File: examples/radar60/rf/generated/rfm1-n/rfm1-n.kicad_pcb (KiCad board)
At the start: 6 copper layers, 31.8 x 23.1 mm, 9 parts, among them U1 IWR6843AQGABLR (rings 0-2 of 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

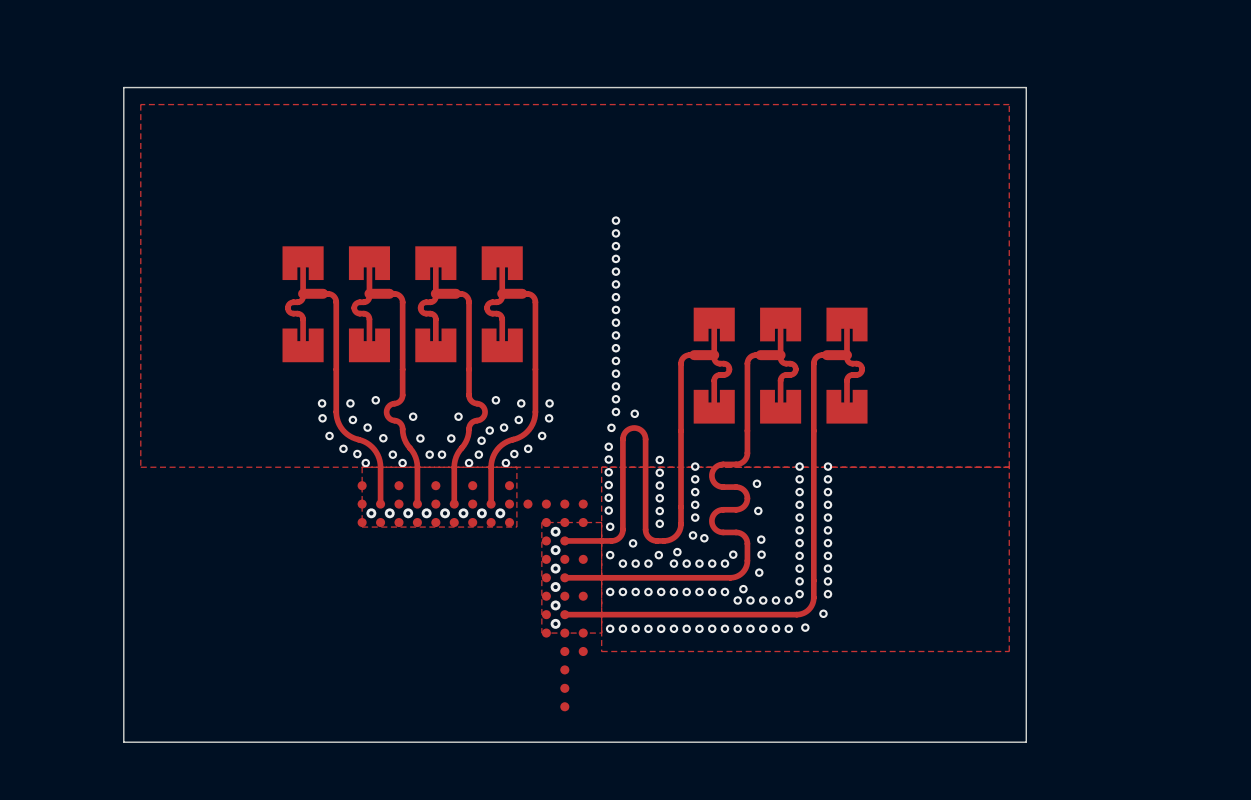
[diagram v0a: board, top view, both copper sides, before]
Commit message: radar60 rf: openEMS first validation and full-wave patch calibration
First EM validation of the conventional column (two patches on L2
windows, corporate divider, gap input) in openEMS v0.37.0-rc3 on the
Mac (Docker, 4 threads, 1.25 M cells, about 14 min per run; no GCP):

- as drawn from closed form the patch resonates at 60.0 GHz, not
  62.05 (-3.3 %), and the column never reaches RL 10 dB (best 9.2 dB at
  60.2 GHz); realized broadside gain 0.0 dBi at 62.05 GHz (7.4 at 60.3)
  against 9.2 dBi predicted;
- a via ring round each window (L2-L3 stitching) does not help;
- a three-point single-patch sweep (L x0.967, inset 0.30/0.38/0.45,
  picked by |S11| at 62.05 GHz) matches the patch (RL >= 10 dB
  60.90-62.80 GHz, -26.9 dB at 61.9 GHz); the column with it reaches
  6.3 / 7.7 / 6.9 dBi realized gain at 60.3 / 62.05 / 63.8 GHz,
  directivity 9.4 dBi, radiation efficiency 70-78 %, but its input is
  still mismatched in band (RL 5.9 / 9.1 / 11.4 dB), which C1 sizes.

The generator now draws L = closed-form L x 0.967 with inset 0.30 mm
(declared parameters citing results/openems/patch-c-i30); the D12
variants bracket the calibrated length. column_sim.py gains a matched
feed (Feed_R 50), a single-patch diagnostic and an optional window via
ring; summarize.py tabulates runs against the closed-form predictions.
All four boards regenerated; KiCad 10.0.6 DRC still reports no
violations and no unconnected items.

Co-Authored-By: Claude Opus 5.5 <noreply@anthropic.com>
Claude-Session: https://claude.ai/code/session_014FiHUDEn5jCP4V8pPjQkPy
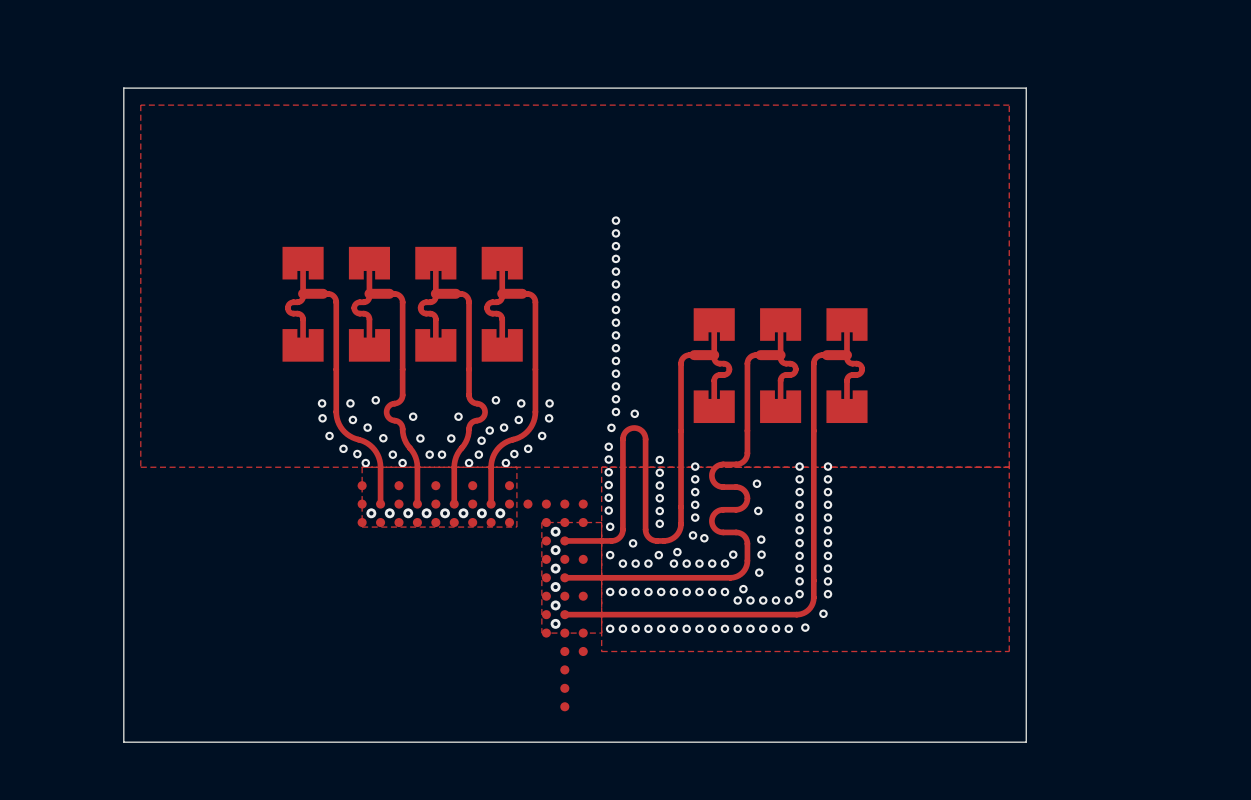
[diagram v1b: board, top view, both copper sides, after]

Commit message: radar60 rf: review fixes (via rules, In2 clip, L2-L3 stitching, placeholder status)
- Fence and isolation vias 0.15/0.32 (the profile's 3 mil ring) with no two vias closer than
  0.43 mm (11 mil hole to hole); the coupon strip likewise. Integration DRC found 288 via and
  2 hole-to-hole violations with the old 0.30 pad and 0.40 spacing.
- In2.Cu GND only where the macro needs its L3 reference: the RF region outside the package,
  the under-package ground of rows 1-3 and A-C, and each land's L2 cut-out plus 0.3 mm. Under
  the rest of the package In2 is the board's escape layer. The outlines go into each record
  (board_frame.in2_gnd_polygons) for the fanout. The macro region now starts at the east pour
  (U1 y -1.3), as the board's RF region does.
- L2-L3 stitching: 208 GND through vias every 0.6 mm (lambda_d/4 in RO4450F at 62 GHz is
  0.64 mm) round each bank (1.4 mm from the patches) and inside the In2 GND boundary. Not
  simulated yet: the C2 bank solve has to report it.
- Every record carries status "placeholder": the column fails ANT-02 RL at P1 (col-c), the
  calibration came from one patch, C1 and C2 come before the macro is frozen.

rfm1-m/-n/-p and the coupon strip: KiCad DRC clean, no unconnected items.

Co-Authored-By: Claude Opus 5.5 <noreply@anthropic.com>
Claude-Session: https://claude.ai/code/session_014FiHUDEn5jCP4V8pPjQkPy
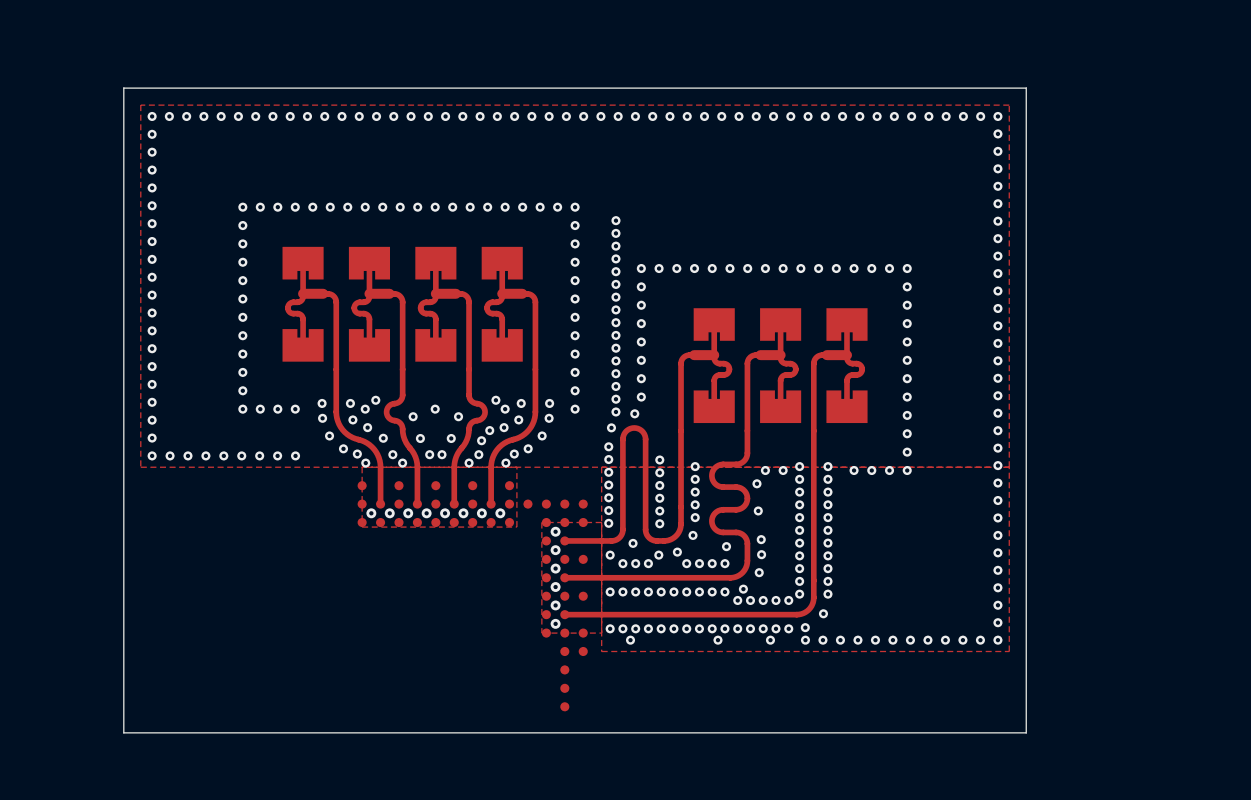
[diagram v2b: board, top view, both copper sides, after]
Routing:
- net GND: vias 158 -> 364
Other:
- board size 31.8 x 23.1 mm -> 31.8 x 22.7 mm

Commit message: radar60 rf: regenerate rfm1-m/n/p and the coupon strip; README
Generator checks pass for all three D12 variants (outside-cut-out hash
identical); kicad-cli pcb drc --refill-zones --severity-all: no
violations, no unconnected items on rfm1-m, -n, -p and the coupon strip.

board_frame (U1 at 26, 28) [D]: RX phase centres y 39.988 (x unchanged),
TX x 38.718 / 41.060 / 43.402 at y 38.100; cut-outs RX 16.599-32.205 x
36.688-43.024, TX 34.205-47.469 x 34.800-41.136; region x 12.599-51.469,
y 26.7-47.024; R4 guard x 7.599-56.469; board height >= 47.349; nearest
active RX-TX phase centres 11.19 mm; loads RL1-RL4.

README: new geometry, the uniformity rules, the checks, the floorplan, the
coupons, the audit and test commands; the integration (kicad_ops) still has
to take the dummy footprints and loads.

Co-Authored-By: Claude Opus 5.5 <noreply@anthropic.com>
Claude-Session: https://claude.ai/code/session_014FiHUDEn5jCP4V8pPjQkPy
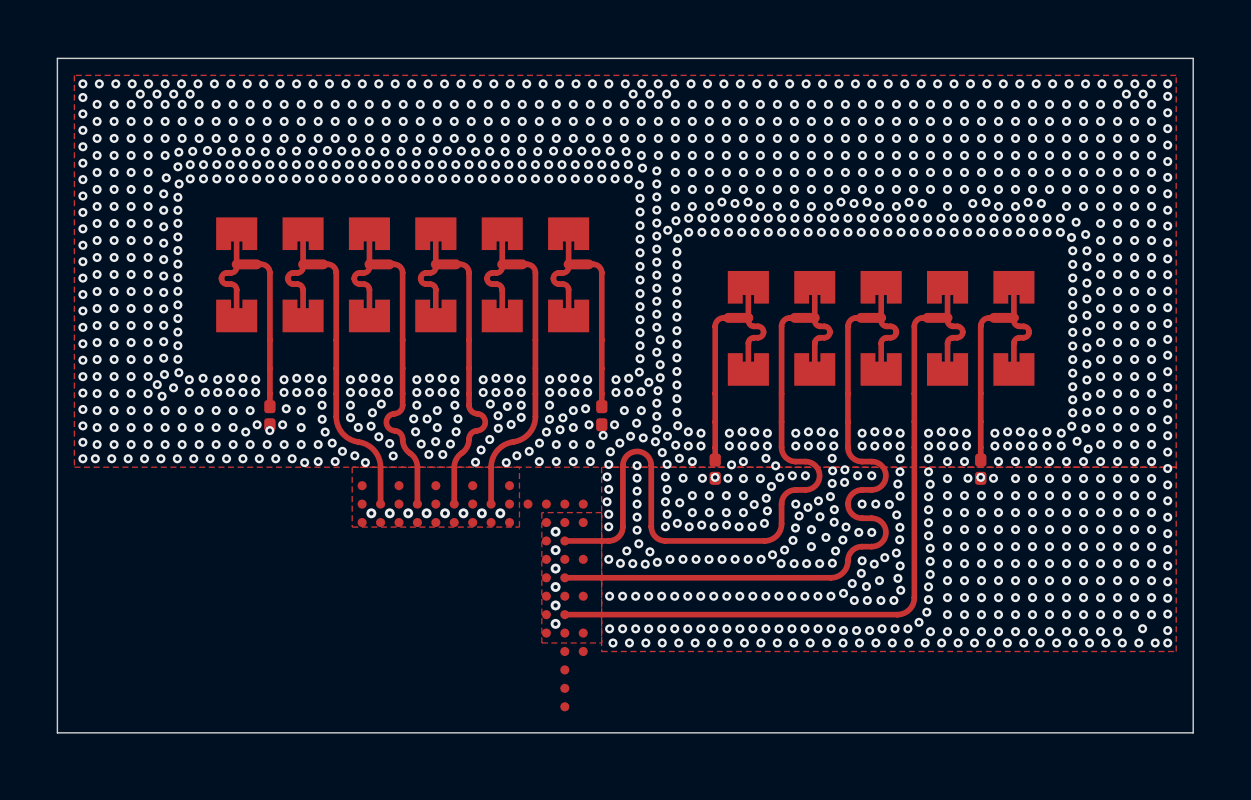
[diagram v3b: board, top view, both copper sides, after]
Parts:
- added ANT_RXD0: 2-patch corporate column, terminated dummy, radar60:COL2_DUMMY, F.Cu at (92.3, 88.0)
- added ANT_RXD5: 2-patch corporate column, terminated dummy, radar60:COL2_DUMMY, F.Cu at (104.0, 88.0)
- added ANT_TXD0: 2-patch corporate column, terminated dummy, radar60:COL2_DUMMY, F.Cu at (110.4, 89.9)
- added ANT_TXD4: 2-patch corporate column, terminated dummy, radar60:COL2_DUMMY, F.Cu at (119.7, 89.9)
- added RL1: 50R 0201 thin film, radar60:R_0201_0603Metric_LOAD, F.Cu at (93.5, 93.0)
- added RL2: 50R 0201 thin film, radar60:R_0201_0603Metric_LOAD, F.Cu at (105.2, 93.0)
- added RL3: 50R 0201 thin film, radar60:R_0201_0603Metric_LOAD, F.Cu at (109.2, 94.9)
- added RL4: 50R 0201 thin film, radar60:R_0201_0603Metric_LOAD, F.Cu at (118.6, 94.9)
- moved ANT_TX1 3.78 mm to (112.7, 89.9)
- moved ANT_TX2 3.78 mm to (115.1, 89.9)
- moved ANT_TX3 3.78 mm to (117.4, 89.9)
- moved ANT_RX1 1.04 mm to (94.7, 88.0)
- moved ANT_RX2 1.04 mm to (97.0, 88.0)
- moved ANT_RX3 1.04 mm to (99.3, 88.0)
- moved ANT_RX4 1.04 mm to (101.7, 88.0)
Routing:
- net RXD0: track 0.00 -> 9.10 mm
- net RXD5: track 0.00 -> 9.10 mm
- net TXD0: track 0.00 -> 9.10 mm
- net TXD4: track 0.00 -> 9.10 mm
- net TX3: track 21.7 -> 26.6 mm
- net TX2: track 21.4 -> 26.2 mm
- net TX1: track 21.6 -> 26.2 mm
- net RX1: track 12.2 -> 13.3 mm
- net RX4: track 12.2 -> 13.3 mm
- net RX2: track 12.1 -> 13.2 mm
- net RX3: track 12.1 -> 13.2 mm
- net GND: vias 364 -> 1443
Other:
- board size 31.8 x 22.7 mm -> 40.1 x 23.8 mm

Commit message: radar60 rf: review fixes of the RF-uniformity layout (loads, G2, G7, audit, coupons)
- Dummy loads: one load cell. Fill vias had landed in three of the four
  0201 GND lands (and differently in each). Each load now has its own five
  vias (pad edges >= 0.14 mm from either land), no other via in its via
  zone, a solder-mask island so the GND land is mask-defined and its vias
  tented, and references RT1-RT4 (RL1/RL2 are the board's radome lands).
  The lands are copper, not pour, for the stitch-reach check. New G7: the
  load cells are identical and no via comes within 0.10 mm of a land.
- G2: the congruence window is symmetric (+-(2d - W/2 - margin)) against
  an interior column. The one declared difference (the absent
  second-neighbour input at an open bank end, RX1 and TX3: 0.95 mm2 of
  copper, 2 vias) is masked and reported.
- Board audit: A1 measures a contact along the cut-out boundary (the x
  extent read TX1's 0.96 mm side contact as 0.05). A2 also compares In1
  and In2 and uses G2's window. New A6: vias at SMD lands. pcbnew is
  imported lazily, so the audits run in the unit tests.
- Regression fixture: the pre-fix rfm1-n (ab57757), KiCad-filled. A1-A4
  must fail on it (RX2/RX3 0.87 mm, TX2 1.48 mm, TX1 two contacts).
- Coupons: CP-T2 (TX2) joins CP-T/CP-T3; without it TX2's corridor was a
  1.3 mm GND channel with a TE10 cut-off near 63 GHz. CP-A gets the
  guard-band rows. The 60 GHz part of the strip is stitched (edge rows,
  0.6 mm grid, fill) and checked like G3. The loads sit under mask islands.
- Regenerated rfm1-m/n/p and the strip. KiCad DRC is clean on all four,
  and A1-A6 pass on the filled m, n and p.

Co-Authored-By: Claude Opus 5.5 <noreply@anthropic.com>
Claude-Session: https://claude.ai/code/session_014FiHUDEn5jCP4V8pPjQkPy
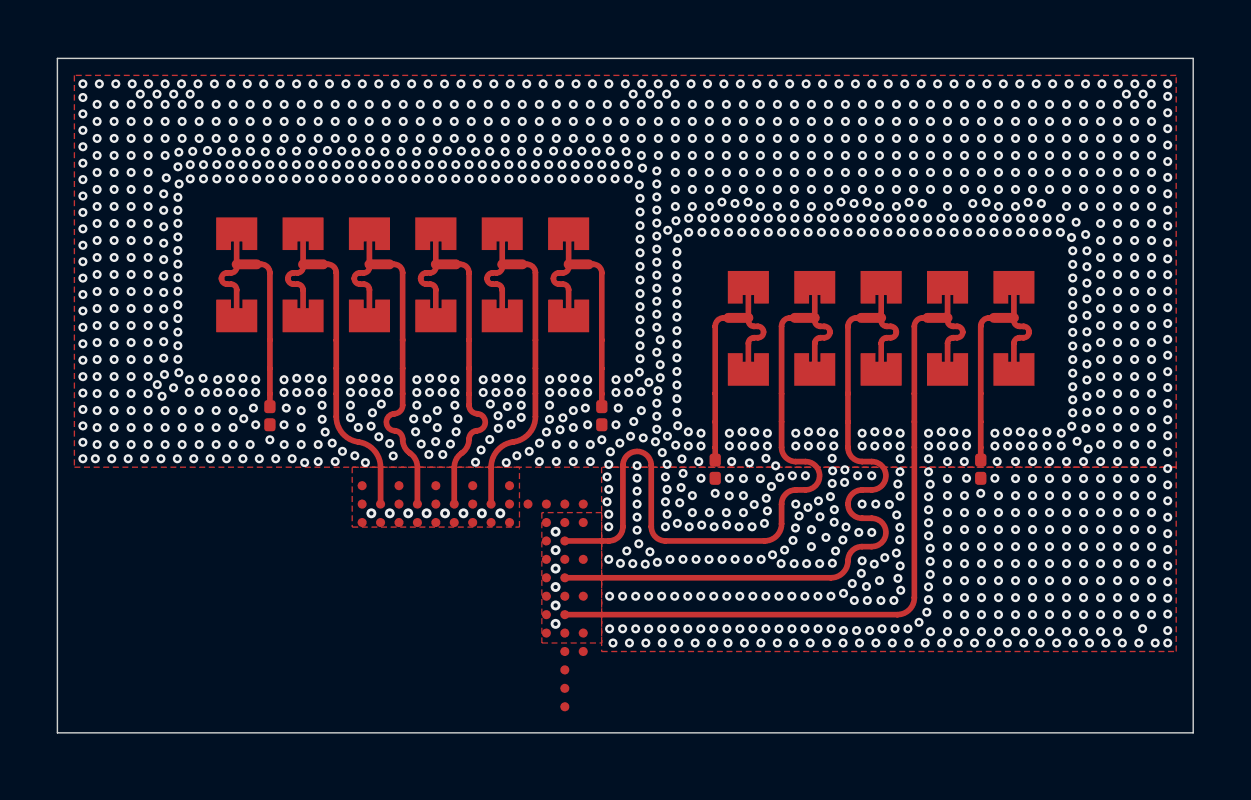
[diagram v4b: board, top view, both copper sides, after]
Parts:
- removed RL1, RL2, RL3, RL4: 50R 0201 thin film, radar60:R_0201_0603Metric_LOAD
- added RT1: 50R 0201 thin film, radar60:R_0201_0603Metric_LOAD, F.Cu at (93.5, 93.0)
- added RT2: 50R 0201 thin film, radar60:R_0201_0603Metric_LOAD, F.Cu at (105.2, 93.0)
- added RT3: 50R 0201 thin film, radar60:R_0201_0603Metric_LOAD, F.Cu at (109.2, 94.9)
- added RT4: 50R 0201 thin film, radar60:R_0201_0603Metric_LOAD, F.Cu at (118.6, 94.9)
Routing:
- net GND: vias 1443 -> 1441

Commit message: radar60 rf: stage 3b generator options, D14 PA feed, D15 pour variants, E1 models
Generator (examples/radar60/rf/rfmacro):
- D14: the macro owns the VOUT_PA (1V0_PA) feed: A2/B2 bar, a neck east of row A
  inside the package outline, four 0.20/0.40 vias in the pocket (board rules
  unchanged; PWR clearance 0.15 mm), an In3 tie stand-in, board_frame.pa_feed
  hand-off (skip_pads A2/B2). New check G8: clearances, pocket, L2 anti-pads,
  current per via, IR drop [D].
- D15: pour presets A (0.60 mm grid), B (1.00 mm grid, interior hard maximum
  0.75 mm), C (GCPW strips, rings, isolation, load cells; L2-L3 lattice). G3 has
  edge and interior thresholds and an L2-L3 check; stitch metrics per record.
- Dummies S1 / S1.5 and DNP loads ("short" refused); G2 declares the edge
  columns S1 leaves without a neighbour.
- L2-L3 cavity options K0 / K2 (posts, column-congruent) / K1; check G9.
- C1 / D5: div_l_scale and a series-fed column in the bank.
- TX: T2 (R 0.75 north-west finger), T4 (TX1 within a skew budget), T3 order
  planarity; the fit keeps lines out of load mask islands.
- Via placement closes fence gaps a shared row leaves (chain shift, row
  re-plan); known limit: T2's lane-finger junction keeps a 0.65 mm gap (G4).
- `rfmacro variants`: the 14 stage-3b boards; rfm1-m/n/p and coupons rebuilt.

EM (openems): triplet / centre-only cells from the generator, plane-pair
ring-down (board_pp, pp_sim), PA corner (board_pa, pa_sim), mesh templates
(ant_sim --mesh-ref), the E1 campaign builder (stage3b_em.py), results/stage3b.

Co-Authored-By: Claude Opus 5.5 <noreply@anthropic.com>
Claude-Session: https://claude.ai/code/session_014FiHUDEn5jCP4V8pPjQkPy
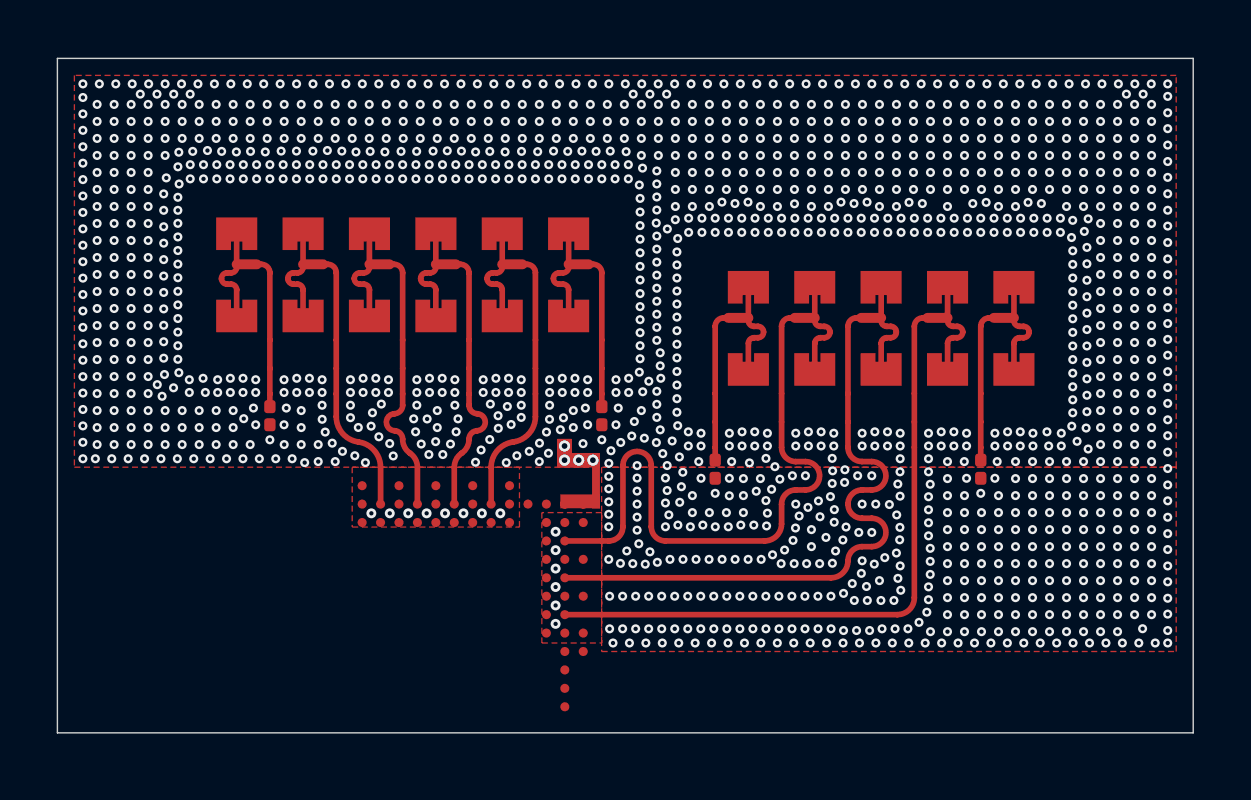
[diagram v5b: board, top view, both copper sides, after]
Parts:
- added PA1: VOUT_PA feed (D14), radar60:RFM1_PA_FEED, F.Cu at (100.0, 100.0)
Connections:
- U1 pad A2: EXT_VOUT_PA_A2 -> 1V0_PA
- U1 pad B2: EXT_VOUT_PA_B2 -> 1V0_PA
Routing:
- net GND: vias 1441 -> 1437
- net 1V0_PA: vias 0 -> 4
- added copper zone on In3.Cu, net 1V0_PA
